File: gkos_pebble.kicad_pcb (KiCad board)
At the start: 4 copper layers, 2 x 10.4 mm, 121 parts, among them IC1 RT8096AHGJ5, IC2 TLV61070A, IC3 RP2040, J1 10129383-906002BLF, J2 217183-0001, J3 BM03B-SRSS-TB, J4 TPS43, J5 LS013B7DH03, Q1 SSM3J35AMFV, SW1 D2LS-21, SW10 EVQ-Q2H03W, SW11 RKB2SJM250SMTR, SW12 RKB2SJM250SMTR, SW13 RKB2SJM250SMTR, SW2 D2LS-21, SW3 D2LS-21, SW4 D2LS-21, SW5 D2LS-21, SW6 D2LS-21, SW7 EVQ-Q2H03W, SW8 EVQ-Q2H03W, SW9 EVQ-Q2H03W, U1 W25Q64JVZPIQ, Y1 ABM3B-12.000MHZ-10-1-U-T, Y2 FC-135 32.7680KA-AC0

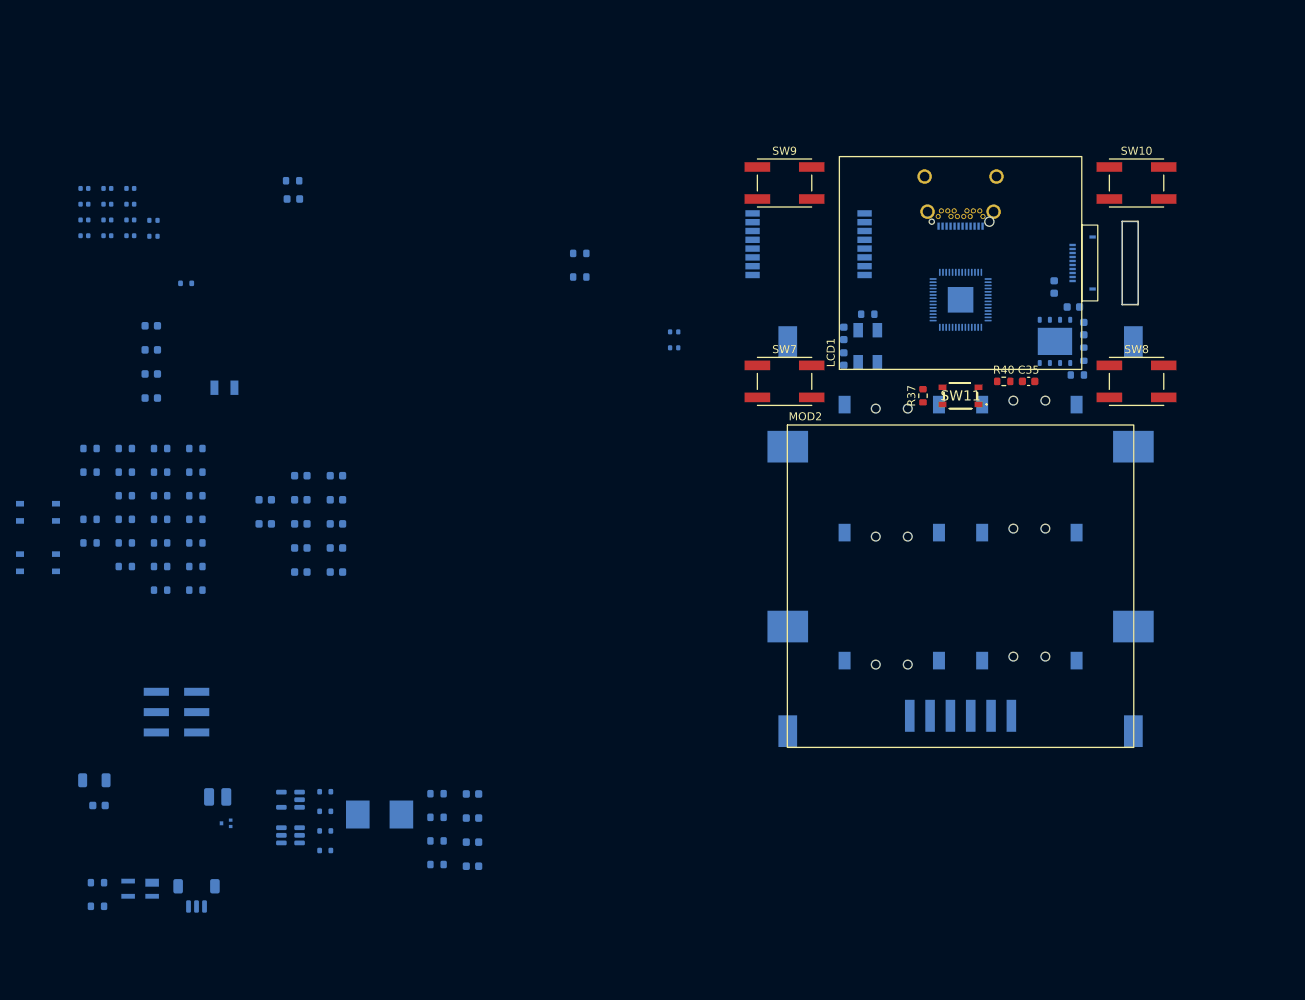
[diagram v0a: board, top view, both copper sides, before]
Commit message: initial component placement on pcb
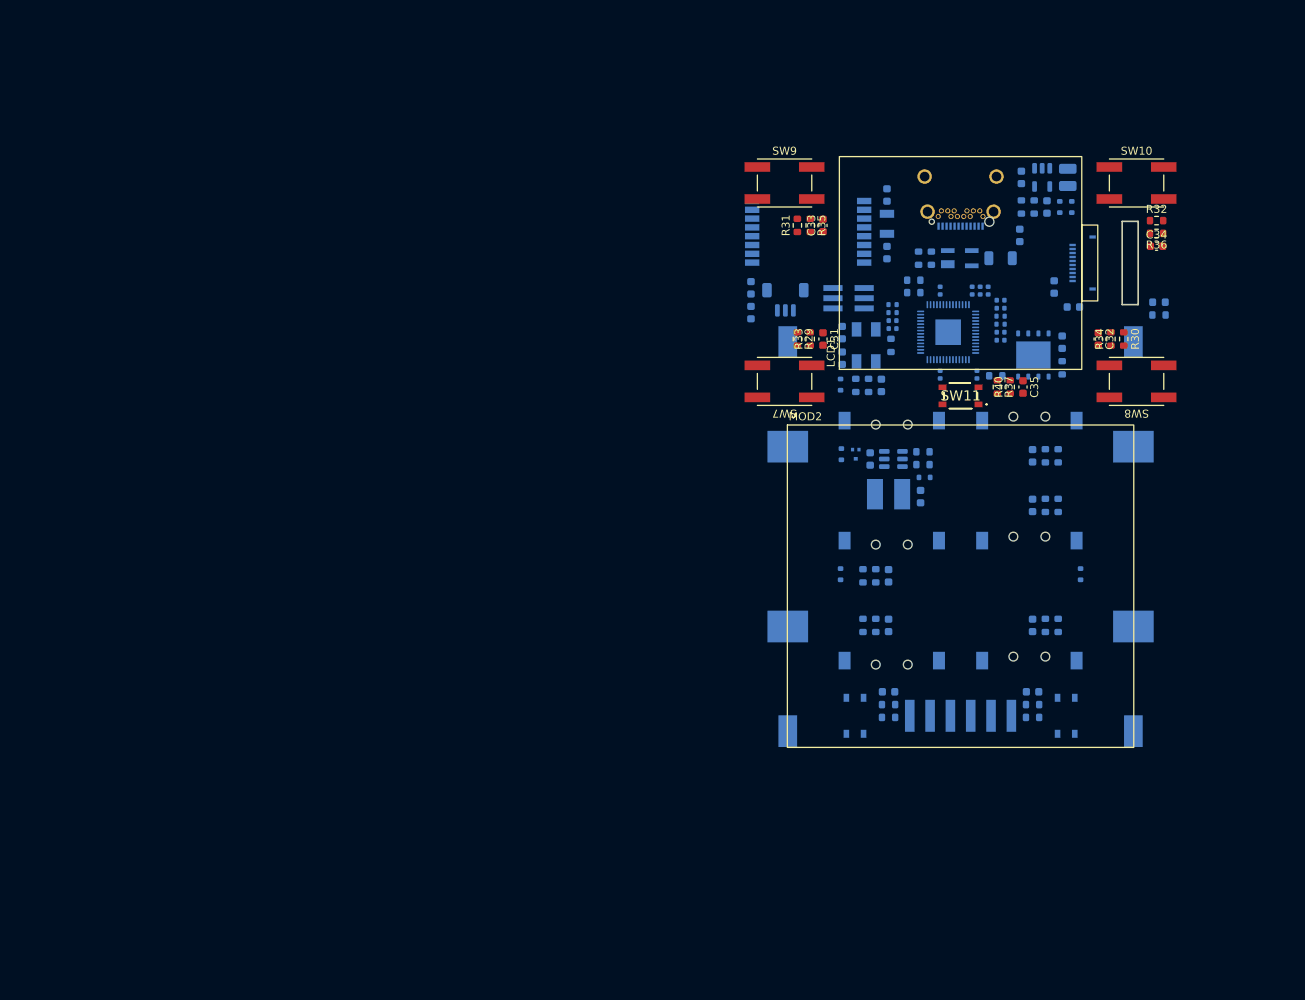
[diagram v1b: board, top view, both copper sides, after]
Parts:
- added D2: LAD52C03L01, Diode_SMD:D_SOD-523, B.Cu at (122.6, 89.1)
- added D9: IN-S63AT5A, LED_SMD:LED_0603_1608Metric, B.Cu at (162.4, 55.1)
- C31, C32, C33, C34, R29, R30, R31, R32, R33, R34, R35, R36: moved to F.Cu
- D4: renamed from D3; value RB521S30 -> LAD52C03L01
- D8: renamed from D7; value IN-S63AT5A -> RB521S30; footprint LED_SMD:LED_0603_1608Metric -> Diode_SMD:D_SOD-523
- J1: value 10129383-906002BLF -> 20021121-00006T4LF; footprint Connector_PinHeader_2.54mm:PinHeader_2x03_P2.54mm_Vertical_SMD -> Connector_PinHeader_1.27mm:PinHeader_2x03_P1.27mm_Vertical_SMD
- L2: footprint Inductor_SMD:L_Bourns_SRP7028A_7.3x6.6mm -> footprints:EXL1V0402-2R2-R
- moved R36 135.5 mm to (162.1, 46.5)
- moved C1 135.4 mm to (145.0, 46.8), turned to 90 degrees
- moved R32 132.7 mm to (162.1, 44.9), turned to 0 degrees
- moved R2 132.0 mm to (133.9, 49.6), turned to -90 degrees
- moved L1 131.5 mm to (151.0, 39.5), turned to -90 degrees
- moved F1 130.7 mm to (142.6, 49.6), turned to 0 degrees
- moved SW13 129.9 mm to (150.8, 106.8), turned to -90 degrees
- moved D1 129.3 mm to (137.5, 49.6), turned to 0 degrees
- moved R1 128.9 mm to (132.3, 49.6), turned to -90 degrees
- moved R34 125.3 mm to (156.4, 59.7), turned to 90 degrees
- moved R30 124.4 mm to (158.0, 59.7), turned to -90 degrees
- moved D6 122.1 mm to (150.0, 43.2), turned to 90 degrees
- moved IC1 122.0 mm to (147.8, 39.5), turned to -90 degrees
- moved R39 121.7 mm to (146.6, 107.0), turned to 0 degrees
- moved R42 119.5 mm to (146.6, 105.4)
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- renumbered D2 to D3, D4 to D5, D5 to D6, D6 to D7
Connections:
- BAT1 pad 2: GND -> Net-(BAT1--)
- BAT2 pad 1: Net-(BAT2-+) -> Net-(BAT1--)
- BAT2 pad 2: Net-(BAT1-+) -> GND
- C5 pad 1: Net-(D5-A) -> Net-(D7-A)
- D3 pad 2: Net-(BAT2-+) -> Net-(BAT1--)
- D4 pad 1: Net-(D3-K) -> GND
- D4 pad 2: Net-(BAT2-+) -> Net-(BAT1-+)
- D5 pad 1: +3V0 -> Net-(D5-K)
- D5 pad 2: +3V3 -> Net-(BAT1-+)
- D6 pad 2: Net-(D5-A) -> +3V3
- D7 pad 1: +3V3 -> +3V0
- D7 pad 2: +3V0 -> Net-(D7-A)
- D8 pad 1: GND -> +3V3
- D8 pad 2: Net-(D7-A) -> +3V0
- IC2 pad 5: Net-(D5-A) -> Net-(D7-A)
- IC3 pad 11: Net-(IC3-GPIO8) -> /inputs/MOUSE_1
- IC3 pad 12: /inputs/KEY_A -> /inputs/MOUSE_2
- IC3 pad 13: /inputs/KEY_B -> /inputs/MOUSE_3
- IC3 pad 14: /inputs/KEY_C -> /inputs/MOUSE_4
- IC3 pad 15: /inputs/MENU -> Net-(IC3-GPIO12)
- IC3 pad 2: /SDA -> /inputs/KEY_A
- IC3 pad 27: Net-(IC3-GPIO16) -> /SDA
- IC3 pad 28: /inputs/TP_RDY -> /SCL
- IC3 pad 29: /inputs/KEY_D -> Net-(IC3-GPIO18)
- IC3 pad 3: /SCL -> /inputs/KEY_B
- IC3 pad 30: /inputs/KEY_E -> Net-(IC3-GPIO19)
- IC3 pad 31: /inputs/KEY_F -> Net-(IC3-GPIO20)
- IC3 pad 34: /lcd/LCD_SCLK -> Net-(IC3-GPIO22)
- IC3 pad 35: /lcd/LCD_SI -> Net-(IC3-GPIO23)
- IC3 pad 36: /lcd/LCD_COMIN -> Net-(IC3-GPIO24)
- IC3 pad 37: /lcd/LCD_SCS -> Net-(IC3-GPIO25)
- IC3 pad 38: Net-(IC3-GPIO26_ADC0) -> /lcd/LCD_SCLK
- IC3 pad 39: Net-(IC3-GPIO27_ADC1) -> /lcd/LCD_SI
- IC3 pad 4: Net-(IC3-GPIO2) -> /inputs/KEY_C
- IC3 pad 40: /inputs/MOUSE_3 -> /lcd/LCD_COMIN
- IC3 pad 41: /inputs/MOUSE_4 -> /lcd/LCD_SCS
- IC3 pad 5: Net-(IC3-GPIO3) -> /inputs/KEY_D
- IC3 pad 6: Net-(IC3-GPIO4) -> /inputs/KEY_E
- IC3 pad 7: Net-(IC3-GPIO5) -> /inputs/KEY_F
- IC3 pad 8: /inputs/MOUSE_1 -> /inputs/MENU
- IC3 pad 9: /inputs/MOUSE_2 -> /inputs/TP_RDY
- Q1 pad 2: Net-(D3-K) -> Net-(D5-K)
- R16 pad 2: Net-(D7-A) -> Net-(D9-A)
- R5 pad 1: Net-(D5-A) -> Net-(D7-A)

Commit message: in-progress second layout attempt
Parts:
- added IC4: AT24C01D-STUM-T, Package_TO_SOT_SMD:SOT-23-5, B.Cu at (148.6, 58.7)
- C6, C7: footprint Capacitor_SMD:C_0603_1608Metric -> Capacitor_SMD:C_0402_1005Metric
- R9: footprint Resistor_SMD:R_0603_1608Metric -> Resistor_SMD:R_0402_1005Metric
- Y1: value ABM3B-12.000MHZ-10-1-U-T -> 7M-12.000MEHE-T; footprint Crystal:Crystal_SMD_Abracon_ABM3B-4Pin_5.0x3.2mm -> footprints:7M-12.000MEHE-T
- moved R16 35.8 mm to (168.3, 21.4)
- moved D9 35.8 mm to (168.3, 19.8)
- moved C6 23.6 mm to (146.2, 65.3), turned to -90 degrees
- moved C7 18.6 mm to (140.0, 66.0), turned to 90 degrees
- moved Y1 17.9 mm to (143.1, 65.0), turned to 180 degrees
- moved C8 14.4 mm to (156.7, 47.1)
- moved U1 12.2 mm to (147.1, 49.5)
- moved R38 12.0 mm to (132.0, 95.5), turned to -90 degrees
- moved R39 12.0 mm to (143.2, 95.5), turned to -90 degrees
- moved C16 11.9 mm to (138.9, 65.0), turned to -90 degrees
- moved R13 11.8 mm to (135.9, 65.0), turned to 90 degrees
- moved MOD2 11.8 mm to (126.3, 87.3)
- moved C10 11.7 mm to (137.9, 65.0), turned to -90 degrees
- moved R12 11.7 mm to (136.9, 65.0), turned to 90 degrees
- moved R9 11.6 mm to (140.0, 64.0), turned to 90 degrees
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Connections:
- net Net-(IC3-USB_DM) renamed /mcu/USB_MCU_D-
- net Net-(IC3-USB_DP) renamed /mcu/USB_MCU_D+
- C38 pad 1: Net-(J5-EXTMODE) -> +3V0
- IC3 pad 11: /inputs/MOUSE_1 -> unconnected-(IC3-GPIO8-Pad11)
- IC3 pad 12: /inputs/MOUSE_2 -> unconnected-(IC3-GPIO9-Pad12)
- IC3 pad 13: /inputs/MOUSE_3 -> unconnected-(IC3-GPIO10-Pad13)
- IC3 pad 14: /inputs/MOUSE_4 -> unconnected-(IC3-GPIO11-Pad14)
- IC3 pad 2: /inputs/KEY_A -> /lcd/LCD_SCLK
- IC3 pad 3: /inputs/KEY_B -> /lcd/LCD_SI
- IC3 pad 35: Net-(IC3-GPIO23) -> /mcu/LED
- IC3 pad 38: /lcd/LCD_SCLK -> unconnected-(IC3-GPIO26_ADC0-Pad38)
- IC3 pad 39: /lcd/LCD_SI -> unconnected-(IC3-GPIO27_ADC1-Pad39)
- IC3 pad 4: /inputs/KEY_C -> /lcd/LCD_SCS
- IC3 pad 40: /lcd/LCD_COMIN -> unconnected-(IC3-GPIO28_ADC2-Pad40)
- IC3 pad 41: /lcd/LCD_SCS -> unconnected-(IC3-GPIO29_ADC3-Pad41)
- IC3 pad 5: /inputs/KEY_D -> /lcd/LCD_COMIN
- IC3 pad 6: /inputs/KEY_E -> unconnected-(IC3-GPIO4-Pad6)
- IC3 pad 7: /inputs/KEY_F -> unconnected-(IC3-GPIO5-Pad7)
- IC3 pad 8: /inputs/MENU -> unconnected-(IC3-GPIO6-Pad8)
- IC3 pad 9: /inputs/TP_RDY -> unconnected-(IC3-GPIO7-Pad9)
- J1 pad 1: /SWD_A -> /SWCLK_A
- J1 pad 2: /SWCLK_A -> /SWD_A
- J1 pad 3: /SWD_IN -> /SWCLK_IN
- J1 pad 4: /SWCLK_IN -> /SWD_IN
- J1 pad 5: /SWD_B -> /SWCLK_B
- J1 pad 6: /SWCLK_B -> /SWD_B
- J5 pad 6: Net-(J5-EXTMODE) -> +3V0
- J5 pad 7: Net-(J5-EXTMODE) -> +3V0
- J5 pad 8: Net-(J5-EXTMODE) -> +3V0
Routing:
- net Net-(BAT1--): track 0.00 -> 59.6 mm
- net /SCL: track 0.00 -> 45.9 mm
- net /SDA: track 0.00 -> 45.3 mm
- net /~{EXT_RST}: track 0.00 -> 44.6 mm, vias 0 -> 1
- net /inputs/TP_RDY: track 0.00 -> 43.1 mm
- net /inputs/KEY_C: track 0.00 -> 34.9 mm
- net /inputs/KEY_D: track 0.00 -> 34.9 mm
- net /inputs/KEY_E: track 0.00 -> 32.5 mm
- net /inputs/KEY_B: track 0.00 -> 32.5 mm
- net /inputs/~{USB_BOOT}: track 0.00 -> 30.5 mm
- net +3V0: track 0.00 -> 26.8 mm, vias 0 -> 1
- net /SWCLK_B: track 0.00 -> 22.0 mm
- net Net-(D1-Pad4): track 0.00 -> 21.0 mm, vias 0 -> 2
- net /SWD_B: track 0.00 -> 17.8 mm
- net Net-(BAT1-+): track 0.00 -> 17.4 mm
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- added copper zone on B.Cu, net +3V0
- added copper zone on B.Cu, net Net-(BAT1-+)
- added copper zone on B.Cu, net Net-(BAT1--)
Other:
- board size 2 x 10.4 mm -> 63.4 x 81.1 mm

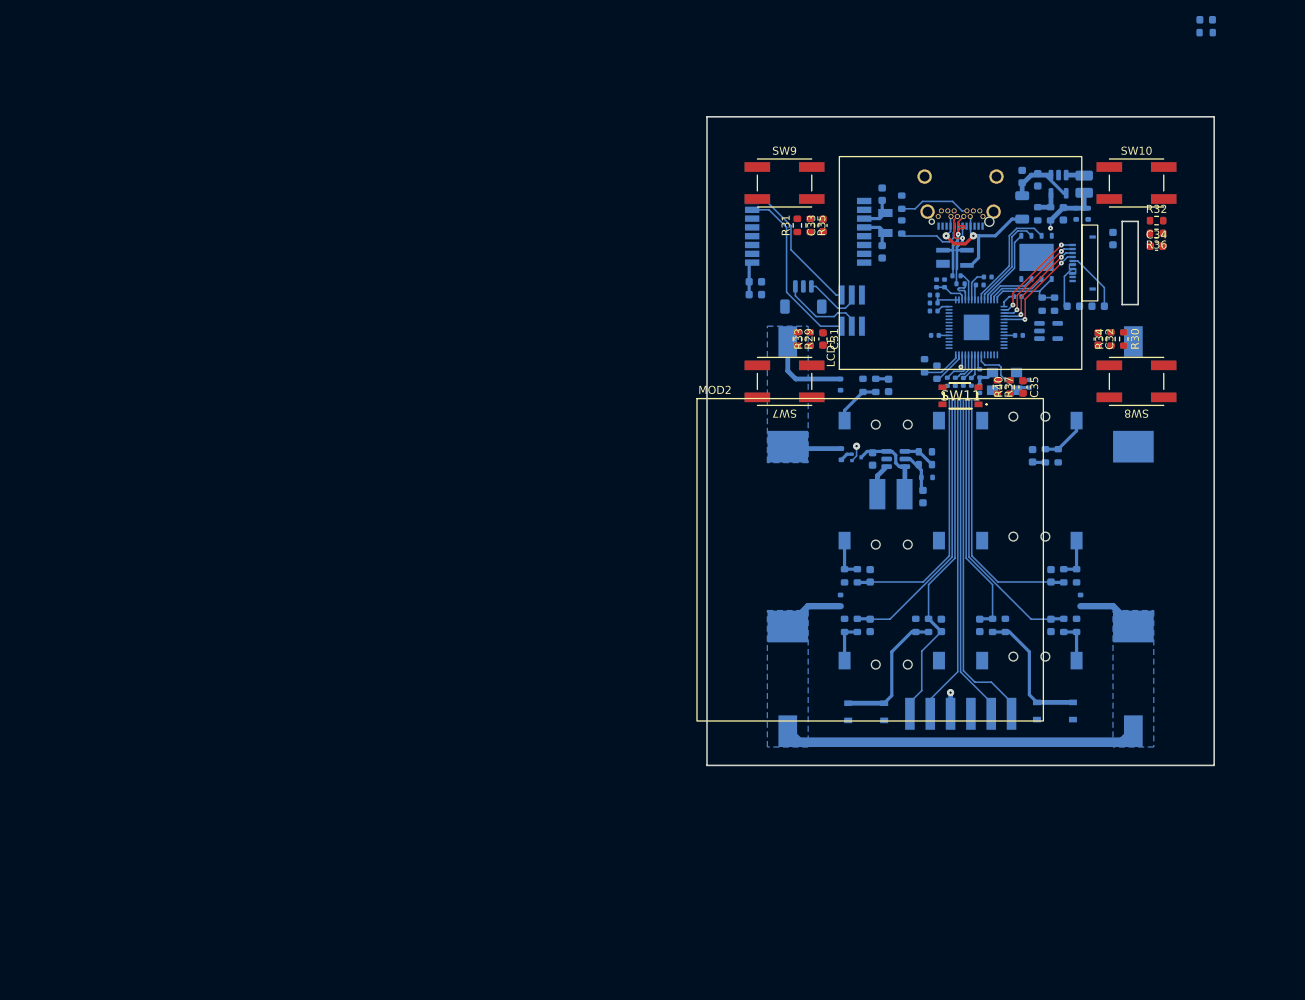
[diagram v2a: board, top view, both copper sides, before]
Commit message: pcb done, also kicad 8
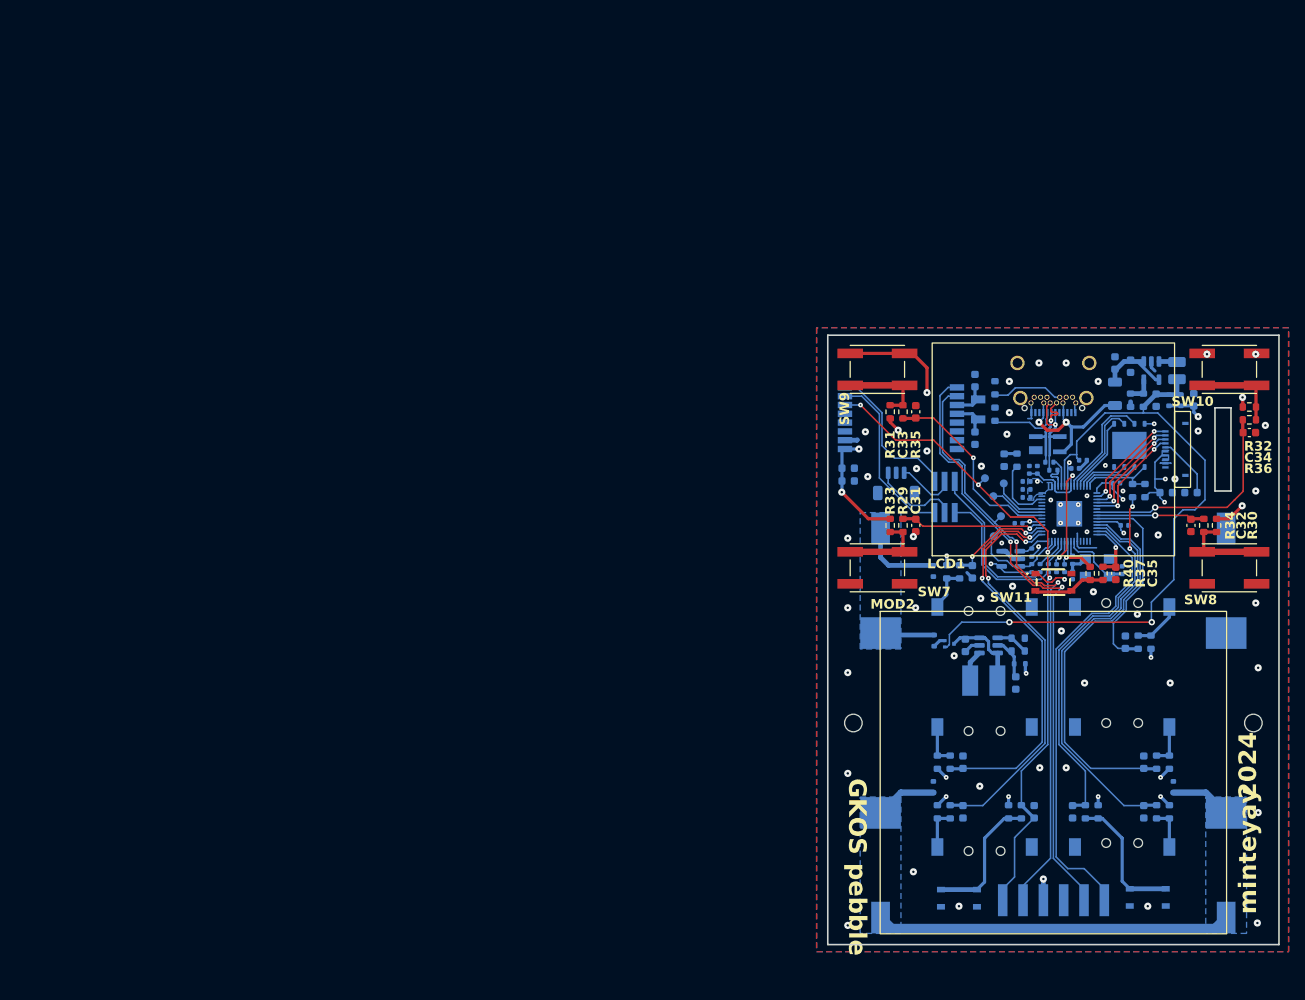
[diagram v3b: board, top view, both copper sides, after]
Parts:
- added H1: M2, MountingHole:MountingHole_2.2mm_M2, F.Cu at (174.2, 107.7)
- added H2: M2, MountingHole:MountingHole_2.2mm_M2, F.Cu at (124.2, 107.7)
- added TP1: RESET, TestPoint:TestPoint_Pad_D1.0mm, B.Cu at (140.7, 77.1)
- added TP2: SDA, TestPoint:TestPoint_Pad_D1.0mm, B.Cu at (141.8, 84.3)
- added TP3: SCL, TestPoint:TestPoint_Pad_D1.0mm, B.Cu at (142.7, 81.8)
- added TP4: GP24, TestPoint:TestPoint_Pad_D1.0mm, B.Cu at (141.7, 79.3)
- added TP5: GP25, TestPoint:TestPoint_Pad_D1.0mm, B.Cu at (143.0, 77.8)
- R14, R15: footprint Resistor_SMD:R_0603_1608Metric -> Resistor_SMD:R_0402_1005Metric
- moved D9 60.6 mm to (143.1, 74.8), turned to 90 degrees
- moved R16 58.4 mm to (144.7, 74.8), turned to 90 degrees
- moved MOD2 35.1 mm to (149.2, 113.9)
- moved IC5 28.9 mm to (143.9, 87.2), turned to 180 degrees
- moved R14 27.2 mm to (146.5, 88.3), turned to 90 degrees
- moved C17 27.2 mm to (158.1, 83.0)
- moved R15 26.9 mm to (146.5, 86.4), turned to 90 degrees
- moved C18 26.3 mm to (157.1, 77.7)
- moved IC3 26.2 mm to (158.7, 73.0)
- moved R2 26.1 mm to (141.9, 69.1)
- moved C10 26.1 mm to (149.6, 88.3)
- moved C16 26.1 mm to (150.6, 88.3)
- moved R12 26.0 mm to (148.6, 88.3)
- moved D5 26.0 mm to (134.3, 97.4)
- moved C38 26.0 mm to (163.3, 78.9)
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- renumbered U1 to IC3, IC3 to IC4, IC4 to IC5
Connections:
- IC4 pad 11: unconnected-(IC3-GPIO8-Pad11) -> /inputs/KEY_E
- IC4 pad 12: unconnected-(IC3-GPIO9-Pad12) -> /inputs/KEY_D
- IC4 pad 13: unconnected-(IC3-GPIO10-Pad13) -> /inputs/TP_RDY
- IC4 pad 14: unconnected-(IC3-GPIO11-Pad14) -> /inputs/MENU
- IC4 pad 15: Net-(IC3-GPIO12) -> unconnected-(IC4-GPIO12-Pad15)
- IC4 pad 16: Net-(IC3-GPIO13) -> unconnected-(IC4-GPIO13-Pad16)
- IC4 pad 17: Net-(IC3-GPIO14) -> unconnected-(IC4-GPIO14-Pad17)
- IC4 pad 18: Net-(IC3-GPIO15) -> unconnected-(IC4-GPIO15-Pad18)
- IC4 pad 29: Net-(IC3-GPIO18) -> /inputs/KEY_C
- IC4 pad 30: Net-(IC3-GPIO19) -> /inputs/KEY_B
- IC4 pad 31: Net-(IC3-GPIO20) -> /inputs/KEY_A
- IC4 pad 32: Net-(IC3-GPIO21) -> /inputs/MOUSE_1
- IC4 pad 34: Net-(IC3-GPIO22) -> unconnected-(IC4-GPIO22-Pad34)
- IC4 pad 35: /mcu/LED -> /inputs/MOUSE_3
- IC4 pad 40: unconnected-(IC3-GPIO28_ADC2-Pad40) -> /mcu/LED
- IC4 pad 7: unconnected-(IC3-GPIO5-Pad7) -> /inputs/MOUSE_4
- IC4 pad 8: unconnected-(IC3-GPIO6-Pad8) -> /inputs/MOUSE_2
- IC4 pad 9: unconnected-(IC3-GPIO7-Pad9) -> /inputs/KEY_F
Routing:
- net +3V3: track 14.2 -> 87.4 mm
- net +3V0: track 26.8 -> 81.5 mm, vias 1 -> 27
- net /SDA: track 45.3 -> 90.1 mm, vias 0 -> 2
- net /~{EXT_RST}: track 44.6 -> 84.8 mm, vias 1 -> 4
- net GND: track 0.00 -> 37.9 mm, vias 0 -> 58
- net /SCL: track 45.9 -> 82.0 mm, vias 0 -> 2
- net /inputs/MOUSE_4: track 0.00 -> 28.3 mm, vias 0 -> 1
- net /inputs/MOUSE_3: track 0.00 -> 24.7 mm, vias 0 -> 1
- net /inputs/KEY_F: track 1.62 -> 25.6 mm
- net /SWD_A: track 0.00 -> 19.7 mm
- net /SWCLK_A: track 0.00 -> 18.5 mm
- net /inputs/MOUSE_1: track 0.00 -> 18.1 mm, vias 0 -> 1
- net /inputs/~{USB_BOOT}: track 30.5 -> 47.1 mm, vias 0 -> 2
- net /inputs/KEY_B: track 32.5 -> 49.1 mm, vias 0 -> 2
- net /inputs/KEY_E: track 32.5 -> 48.8 mm
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- added copper zone on In2.Cu, net +3V0
- added copper zone on B.Cu, net GND
- added copper zone on F.Cu, net GND
- added copper zone on In1.Cu, net GND
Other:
- board size 63.4 x 81.1 mm -> 56.4 x 76.2 mm
- board text added: "0.9-1.8V AAA"
- board text added: "2024"
- board text added: "GKOS pebble"
- board text added: "minteyay"

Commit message: gerbers
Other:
- board text added: "JLCJLCJLCJLC"
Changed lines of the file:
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@@
 		(allow_soldermask_bridges_in_footprints no)
 		(pcbplotparams
-			(layerselection 0x00010fc_ffffffff)
+			(layerselection 0x00010f0_ffffffff)
 			(plot_on_all_layers_selection 0x0000000_00000000)
 			(disableapertmacros no)
@@
 			(usegerberattributes yes)
 			(usegerberadvancedattributes yes)
-			(creategerberjobfile yes)
+			(creategerberjobfile no)
 			(dashed_line_dash_ratio 12.000000)
 			(dashed_line_gap_ratio 3.000000)
@@
 			(plotinvisibletext no)
 			(sketchpadsonfab no)
-			(subtractmaskfromsilk no)
+			(subtractmaskfromsilk yes)
 			(outputformat 1)
 			(mirror no)
-			(drillshape 1)
+			(drillshape 0)
 			(scaleselection 1)
-			(outputdirectory "")
+			(outputdirectory "gerbers/")
 		)
 	)
@@
 		)
 	)
+	(gr_text "JLCJLCJLCJLC"
+		(at 132.6 104.4 0)
+		(layer "F.SilkS")
+		(effects
+			(font
+				(size 1 1)
+				(thickness 0.2)
+				(bold yes)
+			)
+			(justify left bottom)
+		)
+	)
 	(gr_text "minteyay"
 		(at 174.8 131.6 90)
@@
 	)
 	(via
-		(at 174.5 61.6)
+		(at 173.6 63.3)
 		(size 0.9)
 		(drill 0.3)
@@
 	)
 	(via
-		(at 168.4 61.6)
+		(at 168.8 63.3)
 		(size 0.9)
 		(drill 0.3)
